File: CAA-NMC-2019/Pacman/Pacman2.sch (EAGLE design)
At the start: 10 parts, among them IC1 ATTINY85-20SU, J1 M20-9980346

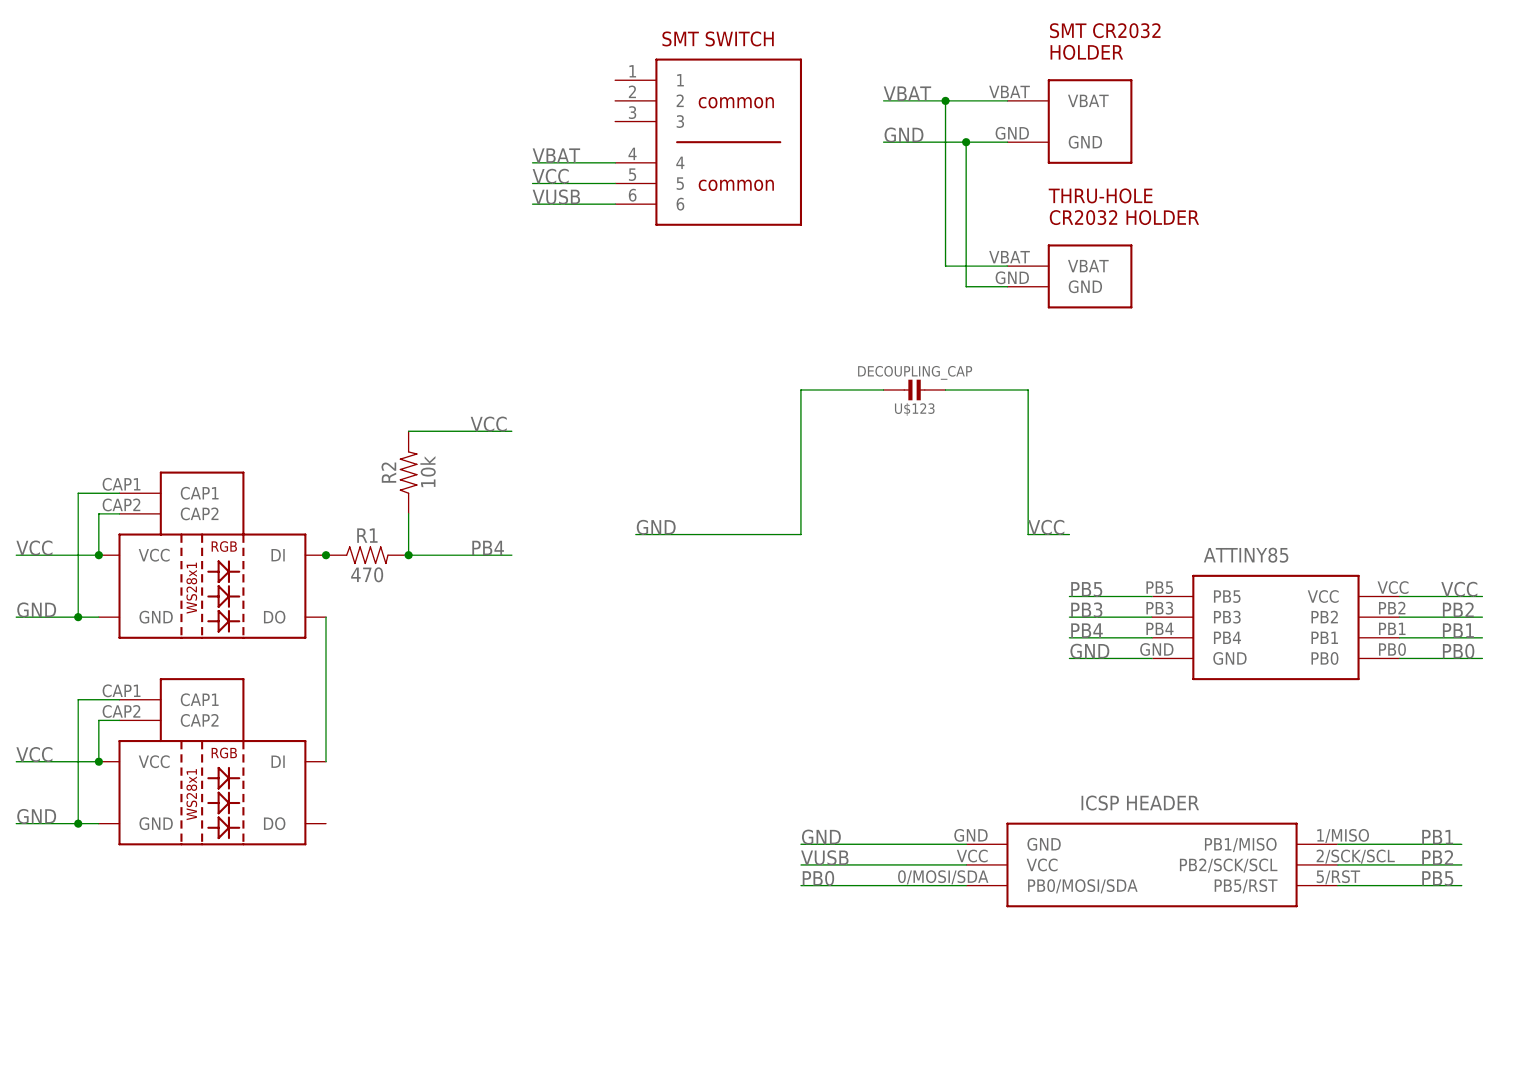
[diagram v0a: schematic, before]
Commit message: visual improvements, replaced cap w/ surface mount
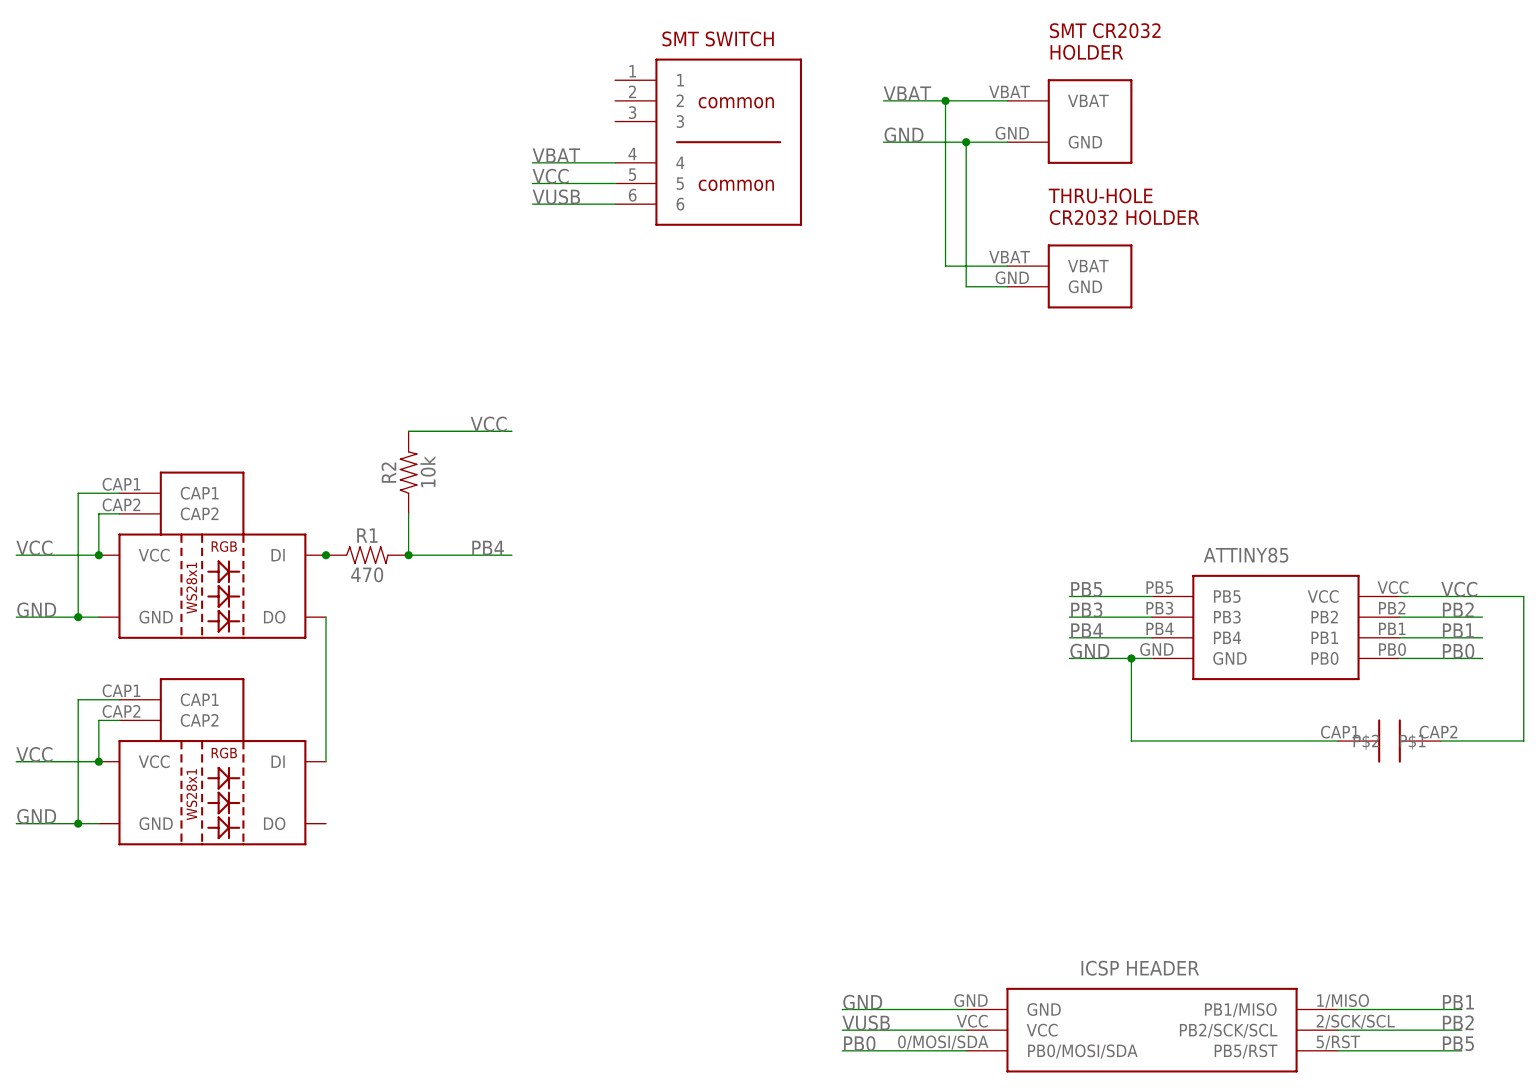
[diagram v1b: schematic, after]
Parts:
- removed J1: M20-9980346, BadgeParts:M20-9980346
- removed U$123: DECOUPLING_CAP, BadgeParts:DECOUPLING_CAP
- added DECOUPLER: .1uf, BadgeParts:0603-CAP
- added J2: ICSP-LO-SILK, BadgeParts:ICSP-LO-SILK
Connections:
- net GND: now also DECOUPLER.P$1, J2.GND; no longer J1.GND, U$123.1
- net PB0: now also J2.PB0/MOSI/SDA; no longer J1.PB0/MOSI/SDA
- net PB1: now also J2.PB1/MISO; no longer J1.PB1/MISO
- net PB2: now also J2.PB2/SCK/SCL; no longer J1.PB2/SCK/SCL
- net PB5: now also J2.PB5/RST; no longer J1.PB5/RST
- net VCC: now also DECOUPLER.P$2; no longer U$123.2
- net VUSB: now also J2.VCC; no longer J1.VCC
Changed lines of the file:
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@@
 <parts>
 <part name="IC1" library="BadgeParts" deviceset="ATTINY85-20SU" device=""/>
-<part name="J1" library="BadgeParts" deviceset="M20-9980346" device=""/>
-<part name="U$123" library="BadgeParts" deviceset="DECOUPLING_CAP" device=""/>
 <part name="U$145" library="BadgeParts" deviceset="SMT-SWITCH" device=""/>
 <part name="D1" library="BadgeParts" deviceset="WS2812B" device="" package3d_urn="urn:adsk.eagle:package:39369/1" value="WS2812B"/>
@@
 <part name="U$2" library="BadgeParts" deviceset="SMT-BATTERY-HOLDER" device=""/>
 <part name="U$3" library="BadgeParts" deviceset="THRU-CR-HOLDER" device=""/>
+<part name="DECOUPLER" library="BadgeParts" deviceset="0603-CAP" device="" value=".1uf"/>
+<part name="J2" library="BadgeParts" deviceset="ICSP-LO-SILK" device=""/>
 </parts>
 <sheets>
@@
 <instances>
 <instance part="IC1" gate="G$1" x="-119.38" y="66.04" smashed="yes"/>
-<instance part="J1" gate="G$1" x="-129.54" y="33.02" smashed="yes"/>
-<instance part="U$123" gate="G$1" x="-147.32" y="91.44" smashed="yes">
-<attribute name="NAME" x="-148.57" y="89.15" size="1.27" layer="95" font="vector" rot="R180" align="center"/>
-<attribute name="VALUE" x="-148.57" y="93.74" size="1.27" layer="96" font="vector" rot="R180" align="center"/>
-</instance>
 <instance part="U$145" gate="G$1" x="-180.34" y="129.54" smashed="yes"/>
 <instance part="D1" gate="G$1" x="-233.68" y="66.04" smashed="yes"/>
@@
 <instance part="U$2" gate="G$1" x="-132.08" y="127" smashed="yes"/>
 <instance part="U$3" gate="G$1" x="-132.08" y="106.68" smashed="yes"/>
+<instance part="DECOUPLER" gate="G$1" x="-88.9" y="48.26" smashed="yes"/>
+<instance part="J2" gate="G$1" x="-129.54" y="12.7" smashed="yes"/>
 </instances>
 <busses>
@@
 </segment>
 <segment>
-<pinref part="J1" gate="G$1" pin="PB0/MOSI/SDA"/>
-<wire x1="-142.24" y1="30.48" x2="-162.56" y2="30.48" width="0.1524" layer="91"/>
-<label x="-162.56" y="30.48" size="1.778" layer="95"/>
+<pinref part="J2" gate="G$1" pin="PB0/MOSI/SDA"/>
+<wire x1="-142.24" y1="10.16" x2="-157.48" y2="10.16" width="0.1524" layer="91"/>
+<label x="-157.48" y="10.16" size="1.778" layer="95"/>
 </segment>
 </net>
 <net name="VCC" class="1">
 <segment>
-<label x="-134.62" y="73.66" size="1.778" layer="95"/>
-<wire x1="-134.62" y1="73.66" x2="-129.54" y2="73.66" width="0.1524" layer="91"/>
-<wire x1="-134.62" y1="91.44" x2="-134.62" y2="73.66" width="0.1524" layer="91"/>
-<pinref part="U$123" gate="G$1" pin="2"/>
-<wire x1="-144.78" y1="91.44" x2="-134.62" y2="91.44" width="0.1524" layer="91"/>
-</segment>
-<segment>
 <pinref part="IC1" gate="G$1" pin="VCC"/>
-<wire x1="-88.9" y1="66.04" x2="-78.74" y2="66.04" width="0.1524" layer="91"/>
+<wire x1="-88.9" y1="66.04" x2="-73.66" y2="66.04" width="0.1524" layer="91"/>
 <label x="-83.82" y="66.04" size="1.778" layer="95"/>
+<pinref part="DECOUPLER" gate="G$1" pin="P$2"/>
+<wire x1="-83.82" y1="48.26" x2="-73.66" y2="48.26" width="0.1524" layer="91"/>
+<wire x1="-73.66" y1="48.26" x2="-73.66" y2="66.04" width="0.1524" layer="91"/>
 </segment>
 <segment>
@@
 <net name="GND" class="2">
 <segment>
-<label x="-182.88" y="73.66" size="1.778" layer="95"/>
-<wire x1="-162.56" y1="73.66" x2="-182.88" y2="73.66" width="0.1524" layer="91"/>
-<wire x1="-162.56" y1="91.44" x2="-162.56" y2="73.66" width="0.1524" layer="91"/>
-<pinref part="U$123" gate="G$1" pin="1"/>
-<wire x1="-162.56" y1="91.44" x2="-152.4" y2="91.44" width="0.1524" layer="91"/>
-</segment>
-<segment>
 <pinref part="IC1" gate="G$1" pin="GND"/>
-<wire x1="-119.38" y1="58.42" x2="-129.54" y2="58.42" width="0.1524" layer="91"/>
+<wire x1="-119.38" y1="58.42" x2="-121.92" y2="58.42" width="0.1524" layer="91"/>
 <label x="-129.54" y="58.42" size="1.778" layer="95"/>
-</segment>
-<segment>
-<pinref part="J1" gate="G$1" pin="GND"/>
-<wire x1="-142.24" y1="35.56" x2="-162.56" y2="35.56" width="0.1524" layer="91"/>
-<label x="-162.56" y="35.56" size="1.778" layer="95"/>
+<pinref part="DECOUPLER" gate="G$1" pin="P$1"/>
+<wire x1="-121.92" y1="58.42" x2="-129.54" y2="58.42" width="0.1524" layer="91"/>
+<wire x1="-96.52" y1="48.26" x2="-121.92" y2="48.26" width="0.1524" layer="91"/>
+<wire x1="-121.92" y1="48.26" x2="-121.92" y2="58.42" width="0.1524" layer="91"/>
+<junction x="-121.92" y="58.42"/>
 </segment>
 <segment>
@@
 <label x="-152.4" y="121.92" size="1.778" layer="95"/>
 </segment>
+<segment>
+<pinref part="J2" gate="G$1" pin="GND"/>
+<wire x1="-142.24" y1="15.24" x2="-157.48" y2="15.24" width="0.1524" layer="91"/>
+<label x="-157.48" y="15.24" size="1.778" layer="95"/>
+</segment>
 </net>
 <net name="PB2" class="0">
@@
 </segment>
 <segment>
-<pinref part="J1" gate="G$1" pin="PB2/SCK/SCL"/>
-<wire x1="-96.52" y1="33.02" x2="-81.28" y2="33.02" width="0.1524" layer="91"/>
-<label x="-86.36" y="33.02" size="1.778" layer="95"/>
+<pinref part="J2" gate="G$1" pin="PB2/SCK/SCL"/>
+<wire x1="-96.52" y1="12.7" x2="-81.28" y2="12.7" width="0.1524" layer="91"/>
+<label x="-83.82" y="12.7" size="1.778" layer="95"/>
 </segment>
 </net>
@@
 </segment>
 <segment>
-<pinref part="J1" gate="G$1" pin="PB5/RST"/>
-<wire x1="-96.52" y1="30.48" x2="-81.28" y2="30.48" width="0.1524" layer="91"/>
-<label x="-86.36" y="30.48" size="1.778" layer="95"/>
+<pinref part="J2" gate="G$1" pin="PB5/RST"/>
+<wire x1="-96.52" y1="10.16" x2="-81.28" y2="10.16" width="0.1524" layer="91"/>
+<label x="-83.82" y="10.16" size="1.778" layer="95"/>
 </segment>
 </net>
@@
 </segment>
 <segment>
-<pinref part="J1" gate="G$1" pin="PB1/MISO"/>
-<wire x1="-96.52" y1="35.56" x2="-81.28" y2="35.56" width="0.1524" layer="91"/>
-<label x="-86.36" y="35.56" size="1.778" layer="95"/>
+<pinref part="J2" gate="G$1" pin="PB1/MISO"/>
+<wire x1="-96.52" y1="15.24" x2="-81.28" y2="15.24" width="0.1524" layer="91"/>
+<label x="-83.82" y="15.24" size="1.778" layer="95"/>
 </segment>
 </net>
@@
 </segment>
 <segment>
-<pinref part="J1" gate="G$1" pin="VCC"/>
-<wire x1="-142.24" y1="33.02" x2="-162.56" y2="33.02" width="0.1524" layer="91"/>
-<label x="-162.56" y="33.02" size="1.778" layer="95"/>
-</segment>
-</net>
+<pinref part="J2" gate="G$1" pin="VCC"/>
+<wire x1="-142.24" y1="12.7" x2="-157.48" y2="12.7" width="0.1524" layer="91"/>
+<label x="-157.48" y="12.7" size="1.778" layer="95"/>
+</segment>
+</net>
